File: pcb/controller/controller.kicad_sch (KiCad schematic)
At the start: 36 parts, among them J1 Barrel_Jack, J2 AVR-ISP-6, U1 ATmega328P-A, Y1 Crystal_GND24

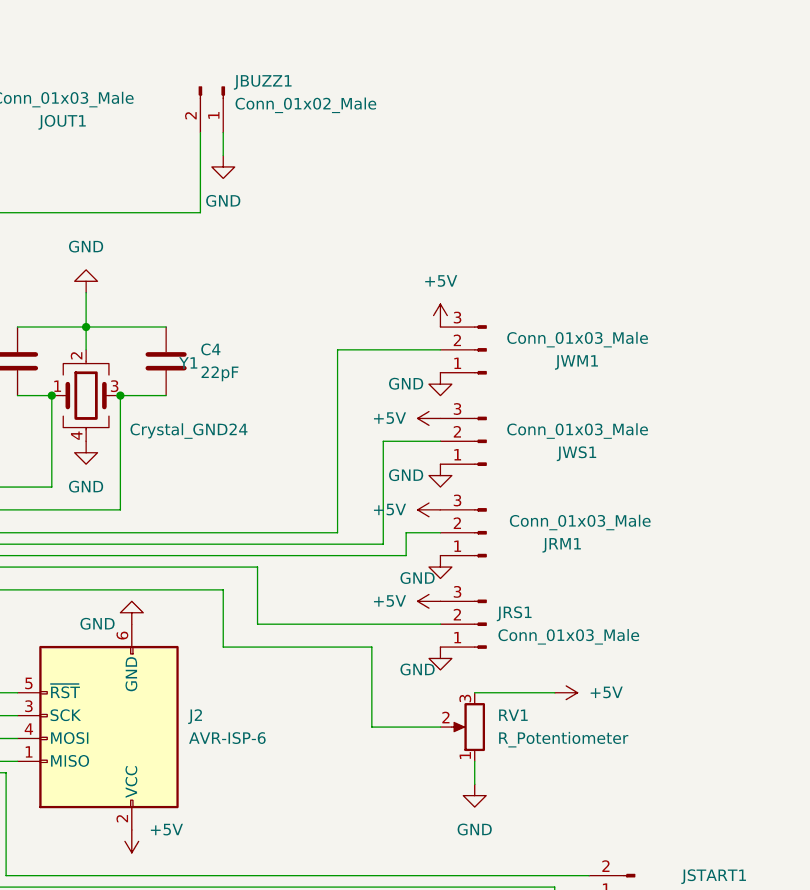
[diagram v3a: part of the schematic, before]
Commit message: Added Volume Control
This adds a volume control potentiometer to the schematic and PCB
design for the control board
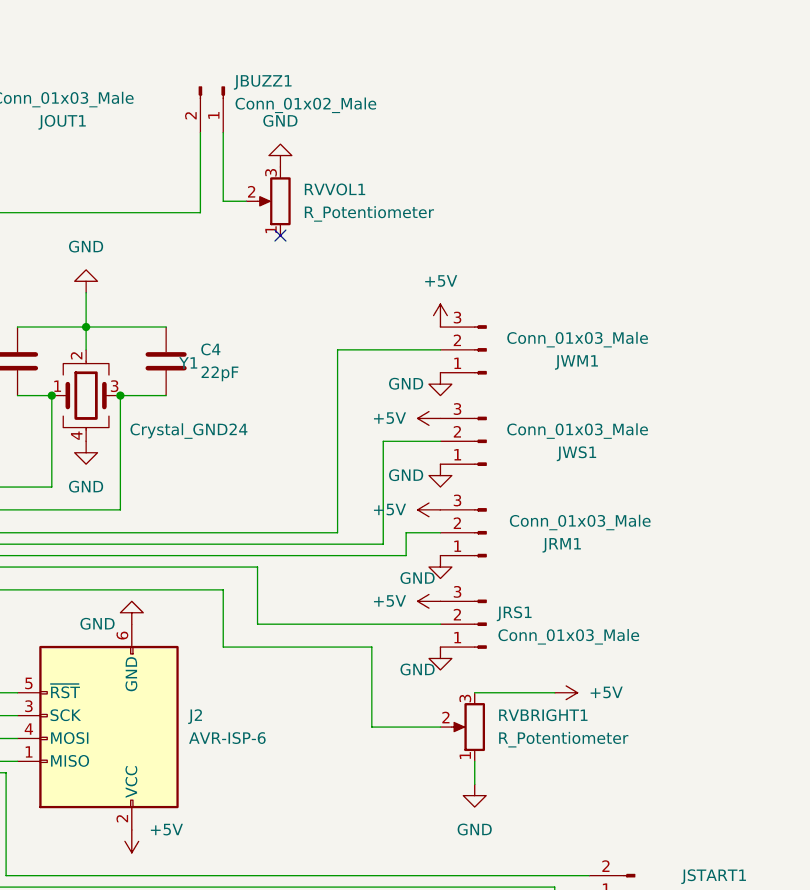
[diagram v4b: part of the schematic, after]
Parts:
- added RVVOL1: R_Potentiometer, Potentiometer_THT:Potentiometer_Bourns_3386P_Vertical, symbol Device:R_Potentiometer
- renumbered RV1 to RVBRIGHT1
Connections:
- net GND: now also RVVOL1.3; no longer JBUZZ1.1 (Pin_1)
- new net: JBUZZ1.1 (Pin_1), RVVOL1.2
- no-connect marks 5 -> 6
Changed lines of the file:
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@@
   (junction (at 92.71 181.61) (diameter 0) (color 0 0 0 0)
   )
+  (no_connect (at 149.86 38.1))
   (no_connect (at 25.4 50.8))
   (no_connect (at 62.23 58.42))
@@
     (stroke (width 0) (type default) (color 0 0 0 0))
   )
-  (wire (pts (xy 143.51 26.67) (xy 143.51 29.21))
+  (wire (pts (xy 143.51 34.29) (xy 146.05 34.29))
     (stroke (width 0) (type default) (color 0 0 0 0))
   )
@@
   )
   (wire (pts (xy 106.68 55.88) (xy 92.71 55.88))
+    (stroke (width 0) (type default) (color 0 0 0 0))
+  )
+  (wire (pts (xy 143.51 26.67) (xy 143.51 34.29))
     (stroke (width 0) (type default) (color 0 0 0 0))
   )
@@
     (pin "2")
   )
+  (symbol (lib_id "Device:R_Potentiometer") (at 149.86 34.29 180) (unit 1)
+    (in_bom yes) (on_board yes)
+    (property "Reference" "RVVOL1" (id 0) (at 152.4 33.0199 0)
+      (effects (font (size 1.27 1.27)) (justify right))
+    )
+    (property "Value" "R_Potentiometer" (id 1) (at 152.4 35.5599 0)
+      (effects (font (size 1.27 1.27)) (justify right))
+    )
+    (property "Footprint" "Potentiometer_THT:Potentiometer_Bourns_3386P_Vertical" (id 2) (at 149.86 34.29 0)
+      (effects (font (size 1.27 1.27)) hide)
+    )
+    (property "Datasheet" "~" (id 3) (at 149.86 34.29 0)
+      (effects (font (size 1.27 1.27)) hide)
+    )
+    (pin "1")
+    (pin "2")
+    (pin "3")
+  )
   (symbol (lib_id "Device:R") (at 91.44 21.59 90) (unit 1)
     (in_bom yes) (on_board yes) (fields_autoplaced)
@@
   (symbol (lib_id "Device:R_Potentiometer") (at 171.45 92.71 180) (unit 1)
     (in_bom yes) (on_board yes) (fields_autoplaced)
-    (property "Reference" "RV1" (id 0) (at 173.99 91.4399 0)
+    (property "Reference" "RVBRIGHT1" (id 0) (at 173.99 91.4399 0)
       (effects (font (size 1.27 1.27)) (justify right))
     )
@@
     (pin "3")
   )
-  (symbol (lib_id "power:GND") (at 143.51 29.21 0) (unit 1)
-    (in_bom yes) (on_board yes) (fields_autoplaced)
-    (property "Reference" "#PWR0118" (id 0) (at 143.51 35.56 0)
-      (effects (font (size 1.27 1.27)) hide)
-    )
-    (property "Value" "GND" (id 1) (at 143.51 34.29 0))
-    (property "Footprint" "" (id 2) (at 143.51 29.21 0)
-      (effects (font (size 1.27 1.27)) hide)
-    )
-    (property "Datasheet" "" (id 3) (at 143.51 29.21 0)
-      (effects (font (size 1.27 1.27)) hide)
-    )
-    (pin "1")
-  )
   (symbol (lib_id "Device:R") (at 102.87 151.13 0) (unit 1)
     (in_bom yes) (on_board yes)
@@
     )
     (property "Datasheet" "" (id 3) (at 171.45 99.06 0)
+      (effects (font (size 1.27 1.27)) hide)
+    )
+    (pin "1")
+  )
+  (symbol (lib_id "power:GND") (at 149.86 30.48 180) (unit 1)
+    (in_bom yes) (on_board yes) (fields_autoplaced)
+    (property "Reference" "#PWR?" (id 0) (at 149.86 24.13 0)
+      (effects (font (size 1.27 1.27)) hide)
+    )
+    (property "Value" "GND" (id 1) (at 149.86 25.4 0))
+    (property "Footprint" "" (id 2) (at 149.86 30.48 0)
+      (effects (font (size 1.27 1.27)) hide)
+    )
+    (property "Datasheet" "" (id 3) (at 149.86 30.48 0)
       (effects (font (size 1.27 1.27)) hide)
     )
@@
       (reference "#PWR0117") (unit 1) (value "GND") (footprint "")
     )
-    (path "/b5b62e28-9fc8-463e-a7f1-aa7597965c9b"
-      (reference "#PWR0118") (unit 1) (value "GND") (footprint "")
-    )
     (path "/7f74c263-cca2-4e4e-8840-c701f7c98d5f"
       (reference "#PWR0119") (unit 1) (value "+5V") (footprint "")
@@
       (reference "#PWR0139") (unit 1) (value "GND") (footprint "")
     )
+    (path "/dfa0e636-84e8-45b2-af70-e06b4d90ce31"
+      (reference "#PWR?") (unit 1) (value "GND") (footprint "")
+    )
     (path "/1259f7ab-f73e-40da-888d-1b2ca8d21b4a"
       (reference "C1") (unit 1) (value ".1uF") (footprint "Capacitor_SMD:C_0603_1608Metric")
@@
     )
     (path "/90473c38-5d7d-4dc8-a497-0758a521fafc"
-      (reference "RV1") (unit 1) (value "R_Potentiometer") (footprint "Potentiometer_THT:Potentiometer_Bourns_3386P_Vertical")
+      (reference "RVBRIGHT1") (unit 1) (value "R_Potentiometer") (footprint "Potentiometer_THT:Potentiometer_Bourns_3386P_Vertical")
+    )
+    (path "/4ef92708-c2d9-4531-af23-a1f9f476bf8c"
+      (reference "RVVOL1") (unit 1) (value "R_Potentiometer") (footprint "Potentiometer_THT:Potentiometer_Bourns_3386P_Vertical")
     )
     (path "/3d2cc86d-e67b-4506-a648-0e934652bff1"

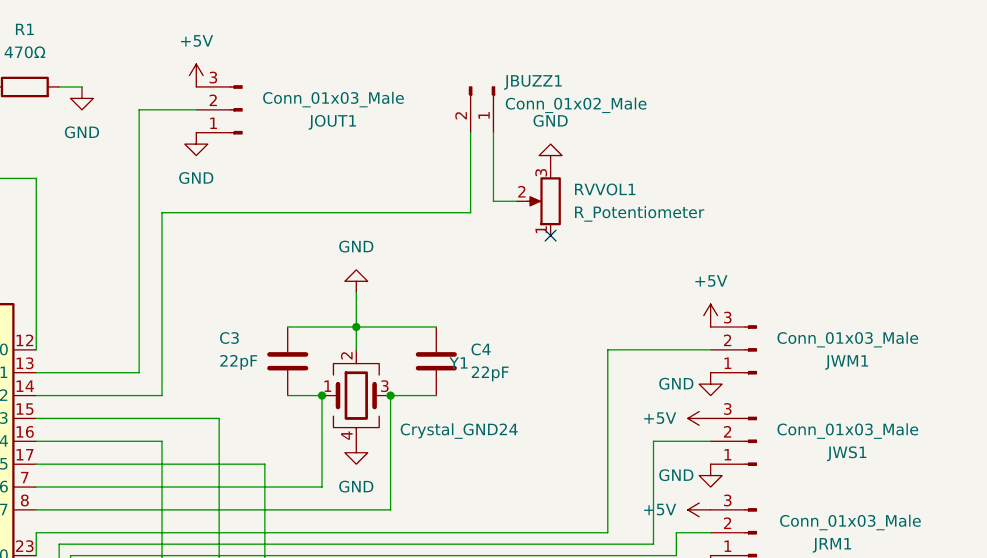
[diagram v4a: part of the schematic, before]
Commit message: Added MOSFET to Controller Board for Buzzer
I want to allow the use of some higher powered piezo buzzers, so this
adds a MOSFET to switch the buzzer current instead of connecting it
directly to the Atmega pin.
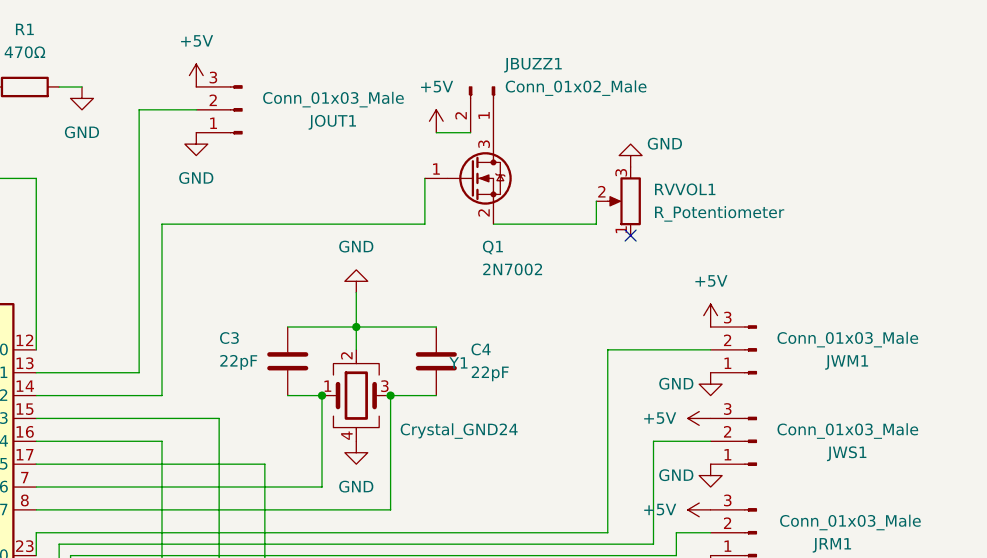
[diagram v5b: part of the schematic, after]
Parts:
- added Q1: 2N7002, Package_TO_SOT_SMD:SOT-23, symbol Transistor_FET:2N7002
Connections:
- net +5V: now also JBUZZ1.2 (Pin_2)
- net at U1.14 (PB2): now also Q1.1 (G); no longer JBUZZ1.2 (Pin_2)
- net at RVVOL1.2: now also Q1.2 (S); no longer JBUZZ1.1 (Pin_1)
- new net: JBUZZ1.1 (Pin_1), Q1.3 (D)
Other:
- moved on the sheet: RVVOL1
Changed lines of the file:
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@@
   (junction (at 92.71 181.61) (diameter 0) (color 0 0 0 0)
   )
-  (no_connect (at 149.86 38.1))
+  (no_connect (at 158.75 38.1))
   (no_connect (at 25.4 50.8))
   (no_connect (at 62.23 58.42))
@@
     (stroke (width 0) (type default) (color 0 0 0 0))
   )
-  (wire (pts (xy 106.68 35.56) (xy 106.68 55.88))
-    (stroke (width 0) (type default) (color 0 0 0 0))
-  )
   (wire (pts (xy 102.87 181.61) (xy 92.71 181.61))
     (stroke (width 0) (type default) (color 0 0 0 0))
@@
     (stroke (width 0) (type default) (color 0 0 0 0))
   )
+  (wire (pts (xy 154.94 36.83) (xy 154.94 34.29))
+    (stroke (width 0) (type default) (color 0 0 0 0))
+  )
   (wire (pts (xy 124.46 128.27) (xy 121.92 128.27))
     (stroke (width 0) (type default) (color 0 0 0 0))
@@
     (stroke (width 0) (type default) (color 0 0 0 0))
   )
-  (wire (pts (xy 143.51 34.29) (xy 146.05 34.29))
-    (stroke (width 0) (type default) (color 0 0 0 0))
-  )
   (wire (pts (xy 118.11 63.5) (xy 118.11 91.44))
     (stroke (width 0) (type default) (color 0 0 0 0))
@@
     (stroke (width 0) (type default) (color 0 0 0 0))
   )
-  (wire (pts (xy 143.51 26.67) (xy 143.51 34.29))
-    (stroke (width 0) (type default) (color 0 0 0 0))
-  )
   (wire (pts (xy 104.14 24.13) (xy 104.14 53.34))
     (stroke (width 0) (type default) (color 0 0 0 0))
@@
     (stroke (width 0) (type default) (color 0 0 0 0))
   )
-  (wire (pts (xy 106.68 35.56) (xy 140.97 35.56))
-    (stroke (width 0) (type default) (color 0 0 0 0))
-  )
   (wire (pts (xy 92.71 63.5) (xy 118.11 63.5))
     (stroke (width 0) (type default) (color 0 0 0 0))
@@
     (stroke (width 0) (type default) (color 0 0 0 0))
   )
+  (wire (pts (xy 106.68 55.88) (xy 106.68 36.83))
+    (stroke (width 0) (type default) (color 0 0 0 0))
+  )
   (wire (pts (xy 138.43 137.16) (xy 130.81 137.16))
     (stroke (width 0) (type default) (color 0 0 0 0))
@@
     (stroke (width 0) (type default) (color 0 0 0 0))
   )
+  (wire (pts (xy 143.51 36.83) (xy 154.94 36.83))
+    (stroke (width 0) (type default) (color 0 0 0 0))
+  )
   (wire (pts (xy 132.08 68.58) (xy 132.08 55.88))
     (stroke (width 0) (type default) (color 0 0 0 0))
@@
     (stroke (width 0) (type default) (color 0 0 0 0))
   )
+  (wire (pts (xy 135.89 36.83) (xy 135.89 31.75))
+    (stroke (width 0) (type default) (color 0 0 0 0))
+  )
   (wire (pts (xy 116.84 111.76) (xy 116.84 100.33))
     (stroke (width 0) (type default) (color 0 0 0 0))
@@
     (stroke (width 0) (type default) (color 0 0 0 0))
   )
+  (wire (pts (xy 137.16 26.67) (xy 140.97 26.67))
+    (stroke (width 0) (type default) (color 0 0 0 0))
+  )
+  (wire (pts (xy 106.68 36.83) (xy 135.89 36.83))
+    (stroke (width 0) (type default) (color 0 0 0 0))
+  )
   (wire (pts (xy 129.54 134.62) (xy 129.54 156.21))
     (stroke (width 0) (type default) (color 0 0 0 0))
@@
   )
   (wire (pts (xy 179.07 111.76) (xy 116.84 111.76))
-    (stroke (width 0) (type default) (color 0 0 0 0))
-  )
-  (wire (pts (xy 140.97 26.67) (xy 140.97 35.56))
     (stroke (width 0) (type default) (color 0 0 0 0))
   )
@@
     (pin "2")
   )
-  (symbol (lib_id "Device:R_Potentiometer") (at 149.86 34.29 180) (unit 1)
-    (in_bom yes) (on_board yes)
-    (property "Reference" "RVVOL1" (id 0) (at 152.4 33.0199 0)
+  (symbol (lib_id "Device:R_Potentiometer") (at 158.75 34.29 180) (unit 1)
+    (in_bom yes) (on_board yes)
+    (property "Reference" "RVVOL1" (id 0) (at 161.29 33.0199 0)
       (effects (font (size 1.27 1.27)) (justify right))
     )
-    (property "Value" "R_Potentiometer" (id 1) (at 152.4 35.5599 0)
+    (property "Value" "R_Potentiometer" (id 1) (at 161.29 35.5599 0)
       (effects (font (size 1.27 1.27)) (justify right))
     )
-    (property "Footprint" "Potentiometer_THT:Potentiometer_Bourns_3386P_Vertical" (id 2) (at 149.86 34.29 0)
-      (effects (font (size 1.27 1.27)) hide)
-    )
-    (property "Datasheet" "~" (id 3) (at 149.86 34.29 0)
+    (property "Footprint" "Potentiometer_THT:Potentiometer_Bourns_3386P_Vertical" (id 2) (at 158.75 34.29 0)
+      (effects (font (size 1.27 1.27)) hide)
+    )
+    (property "Datasheet" "~" (id 3) (at 158.75 34.29 0)
       (effects (font (size 1.27 1.27)) hide)
     )
@@
   )
   (symbol (lib_id "Connector:Conn_01x02_Male") (at 143.51 21.59 270) (unit 1)
-    (in_bom yes) (on_board yes) (fields_autoplaced)
-    (property "Reference" "JBUZZ1" (id 0) (at 144.78 20.9549 90)
-      (effects (font (size 1.27 1.27)) (justify left))
-    )
-    (property "Value" "Conn_01x02_Male" (id 1) (at 144.78 23.4949 90)
+    (in_bom yes) (on_board yes)
+    (property "Reference" "JBUZZ1" (id 0) (at 144.78 19.05 90)
+      (effects (font (size 1.27 1.27)) (justify left))
+    )
+    (property "Value" "Conn_01x02_Male" (id 1) (at 144.78 21.59 90)
       (effects (font (size 1.27 1.27)) (justify left))
     )
@@
     )
     (pin "1")
+  )
+  (symbol (lib_id "Transistor_FET:2N7002") (at 140.97 31.75 0) (unit 1)
+    (in_bom yes) (on_board yes)
+    (property "Reference" "Q1" (id 0) (at 142.24 39.37 0)
+      (effects (font (size 1.27 1.27)) (justify left))
+    )
+    (property "Value" "2N7002" (id 1) (at 142.24 41.91 0)
+      (effects (font (size 1.27 1.27)) (justify left))
+    )
+    (property "Footprint" "Package_TO_SOT_SMD:SOT-23" (id 2) (at 146.05 33.655 0)
+      (effects (font (size 1.27 1.27) italic) (justify left) hide)
+    )
+    (property "Datasheet" "https://www.onsemi.com/pub/Collateral/NDS7002A-D.PDF" (id 3) (at 140.97 31.75 0)
+      (effects (font (size 1.27 1.27)) (justify left) hide)
+    )
+    (property "LCSC" "C8545" (id 4) (at 140.97 31.75 0)
+      (effects (font (size 1.27 1.27)) hide)
+    )
+    (pin "1")
+    (pin "2")
+    (pin "3")
   )
   (symbol (lib_id "Connector:AVR-ISP-6") (at 130.81 91.44 180) (unit 1)
@@
     (pin "2")
   )
+  (symbol (lib_id "power:+5V") (at 137.16 26.67 0) (unit 1)
+    (in_bom yes) (on_board yes) (fields_autoplaced)
+    (property "Reference" "#PWR0118" (id 0) (at 137.16 30.48 0)
+      (effects (font (size 1.27 1.27)) hide)
+    )
+    (property "Value" "+5V" (id 1) (at 137.16 21.59 0))
+    (property "Footprint" "" (id 2) (at 137.16 26.67 0)
+      (effects (font (size 1.27 1.27)) hide)
+    )
+    (property "Datasheet" "" (id 3) (at 137.16 26.67 0)
+      (effects (font (size 1.27 1.27)) hide)
+    )
+    (pin "1")
+  )
   (symbol (lib_id "power:+5V") (at 167.64 78.74 90) (unit 1)
     (in_bom yes) (on_board yes) (fields_autoplaced)
@@
     (pin "1")
   )
-  (symbol (lib_id "power:GND") (at 149.86 30.48 180) (unit 1)
-    (in_bom yes) (on_board yes) (fields_autoplaced)
-    (property "Reference" "#PWR?" (id 0) (at 149.86 24.13 0)
-      (effects (font (size 1.27 1.27)) hide)
-    )
-    (property "Value" "GND" (id 1) (at 149.86 25.4 0))
-    (property "Footprint" "" (id 2) (at 149.86 30.48 0)
-      (effects (font (size 1.27 1.27)) hide)
-    )
-    (property "Datasheet" "" (id 3) (at 149.86 30.48 0)
+  (symbol (lib_id "power:GND") (at 158.75 30.48 180) (unit 1)
+    (in_bom yes) (on_board yes)
+    (property "Reference" "#PWR0140" (id 0) (at 158.75 24.13 0)
+      (effects (font (size 1.27 1.27)) hide)
+    )
+    (property "Value" "GND" (id 1) (at 162.56 27.94 0))
+    (property "Footprint" "" (id 2) (at 158.75 30.48 0)
+      (effects (font (size 1.27 1.27)) hide)
+    )
+    (property "Datasheet" "" (id 3) (at 158.75 30.48 0)
       (effects (font (size 1.27 1.27)) hide)
     )
@@
       (reference "#PWR0117") (unit 1) (value "GND") (footprint "")
     )
+    (path "/a0d84994-373b-480a-9a64-670bd4f15d64"
+      (reference "#PWR0118") (unit 1) (value "+5V") (footprint "")
+    )
     (path "/7f74c263-cca2-4e4e-8840-c701f7c98d5f"
       (reference "#PWR0119") (unit 1) (value "+5V") (footprint "")
@@
     )
     (path "/dfa0e636-84e8-45b2-af70-e06b4d90ce31"
-      (reference "#PWR?") (unit 1) (value "GND") (footprint "")
+      (reference "#PWR0140") (unit 1) (value "GND") (footprint "")
     )
     (path "/1259f7ab-f73e-40da-888d-1b2ca8d21b4a"
@@
       (reference "JWS1") (unit 1) (value "Conn_01x03_Male") (footprint "Connector_JST:JST_PH_B3B-PH-K_1x03_P2.00mm_Vertical")
     )
+    (path "/7681789a-54ff-407c-927c-10c8a7b5fa79"
+      (reference "Q1") (unit 1) (value "2N7002") (footprint "Package_TO_SOT_SMD:SOT-23")
+    )
     (path "/50b4d9f0-1a5d-4592-8fa5-c4c991413255"
